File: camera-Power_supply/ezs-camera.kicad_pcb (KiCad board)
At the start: 2 copper layers, 47 x 51 mm, 42 parts, among them J1 CONN_01X12, J2 CONN_02X12, J3 STEP, J4 POWER, J5 BAT, J6 PWR_LED, U1 ULN2003, U2 BQ2407x, U3 LM3405, U4 TPS6123x

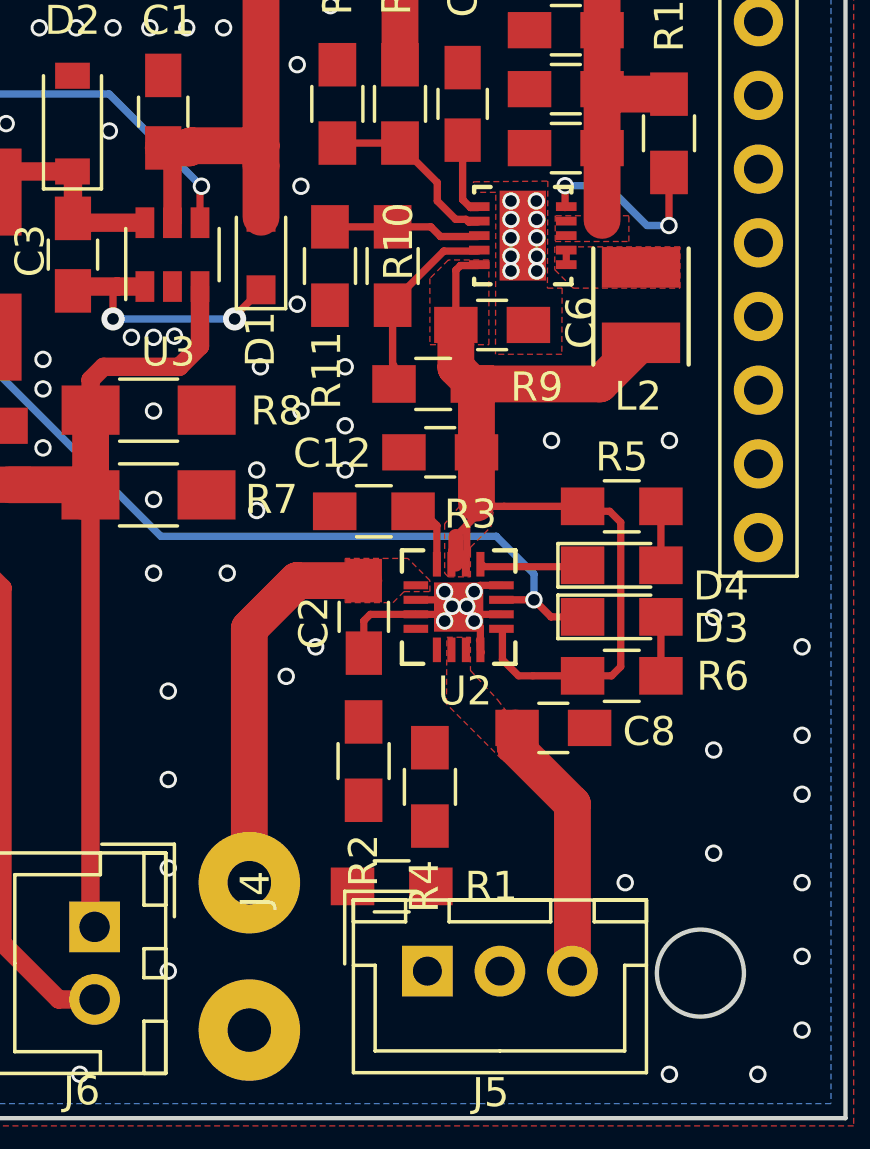
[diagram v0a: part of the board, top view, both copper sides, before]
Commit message: v1.1 redesign
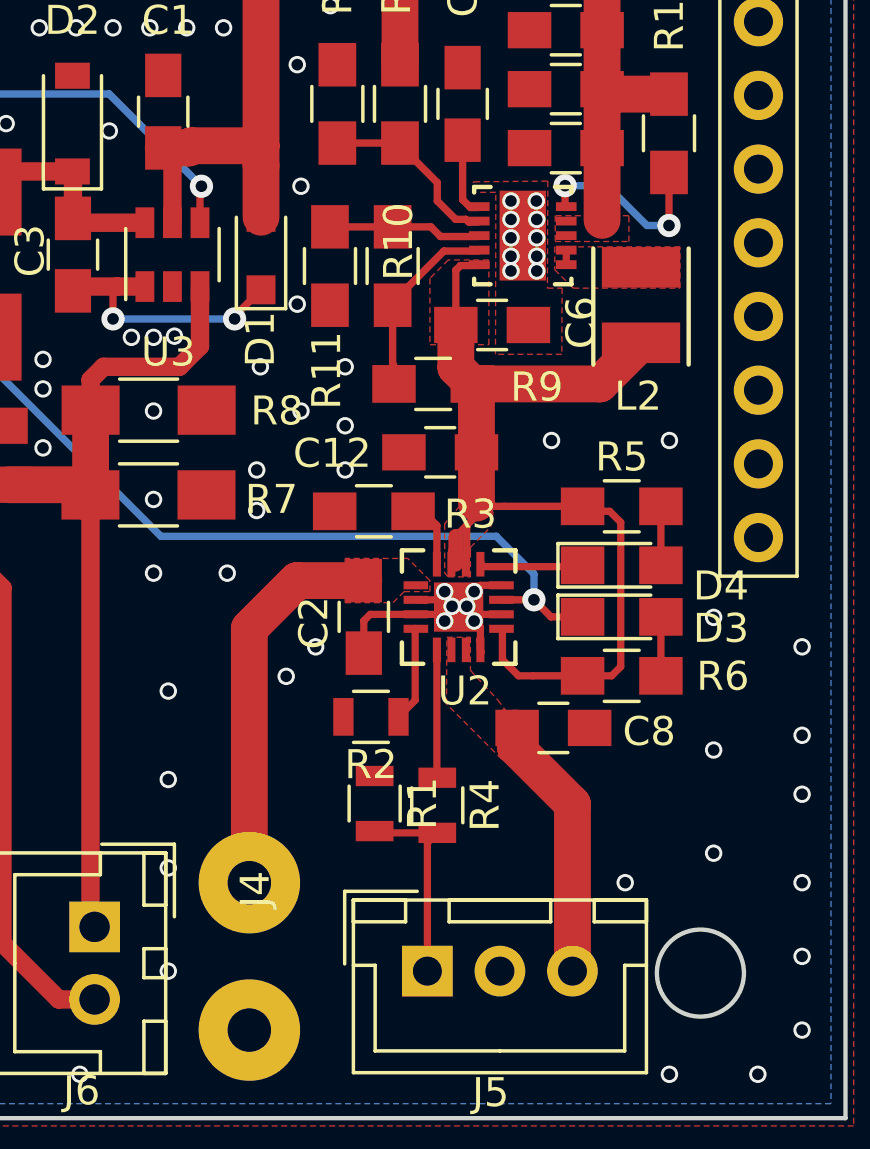
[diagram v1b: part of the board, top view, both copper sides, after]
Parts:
- R1, R2, R4: footprint Resistors_SMD:R_0805_HandSoldering -> Resistors_SMD:R_0805
- moved R1 2.91 mm to (144.3, 148.7), turned to 270 degrees
- moved R2 1.55 mm to (144.1, 145.7), turned to 180 degrees
- moved R4 0.68 mm to (146.4, 148.7)
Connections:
- J1 pad 1: (no net) -> Net-(J1-Pad1)
- J1 pad 10: (no net) -> Net-(J1-Pad10)
- J1 pad 11: (no net) -> Net-(J1-Pad11)
- J1 pad 12: GND -> Net-(J1-Pad12)
- J1 pad 2: (no net) -> Net-(J1-Pad2)
- J1 pad 3: (no net) -> Net-(J1-Pad3)
- J1 pad 4: (no net) -> Net-(J1-Pad4)
- J1 pad 5: (no net) -> Net-(J1-Pad5)
- J1 pad 6: (no net) -> Net-(J1-Pad6)
- J1 pad 7: (no net) -> Net-(J1-Pad7)
- J1 pad 8: (no net) -> Net-(J1-Pad8)
- J1 pad 9: (no net) -> Net-(J1-Pad9)
- J2 pad 1: (no net) -> Net-(J2-Pad1)
- J2 pad 10: (no net) -> Net-(J2-Pad10)
- J2 pad 12: (no net) -> Net-(J2-Pad12)
- J2 pad 16: (no net) -> Net-(J2-Pad16)
- J2 pad 17: (no net) -> Net-(J2-Pad17)
- J2 pad 18: (no net) -> Net-(J2-Pad18)
- J2 pad 22: (no net) -> Net-(J2-Pad22)
- J2 pad 24: (no net) -> Net-(J2-Pad24)
- J2 pad 3: (no net) -> Net-(J2-Pad3)
- J2 pad 5: (no net) -> Net-(J2-Pad5)
- J2 pad 7: (no net) -> Net-(J2-Pad7)
- J2 pad 8: (no net) -> Net-(J2-Pad8)
- U1 pad 10: (no net) -> Net-(U1-Pad10)
- U1 pad 11: (no net) -> Net-(U1-Pad11)
- U1 pad 12: (no net) -> Net-(U1-Pad12)
- U1 pad 5: (no net) -> Net-(U1-Pad5)
- U1 pad 6: (no net) -> Net-(U1-Pad6)
- U1 pad 7: (no net) -> Net-(U1-Pad7)
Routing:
- net Net-(J5-Pad1): track 0.00 -> 7.09 mm
- net Net-(R4-Pad1): track 0.00 -> 4.41 mm
- net Net-(R2-Pad1): track 0.00 -> 3.31 mm
